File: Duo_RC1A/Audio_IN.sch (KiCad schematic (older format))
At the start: 126 parts, among them J1 JACK_P10_TRS_6P, J2 JACK_P10_TRS_6P

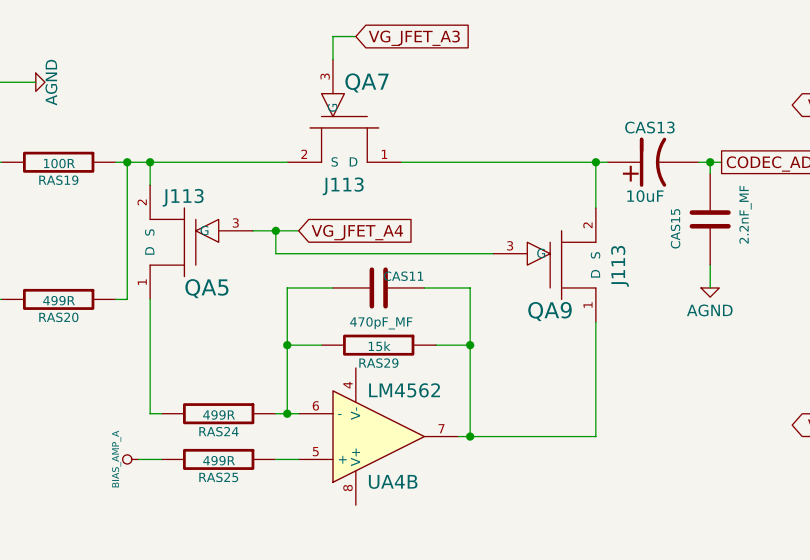
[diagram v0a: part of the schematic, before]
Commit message: PCB dimensions and group placement of all footprints on both BottomBoard and TopBoard layouts.
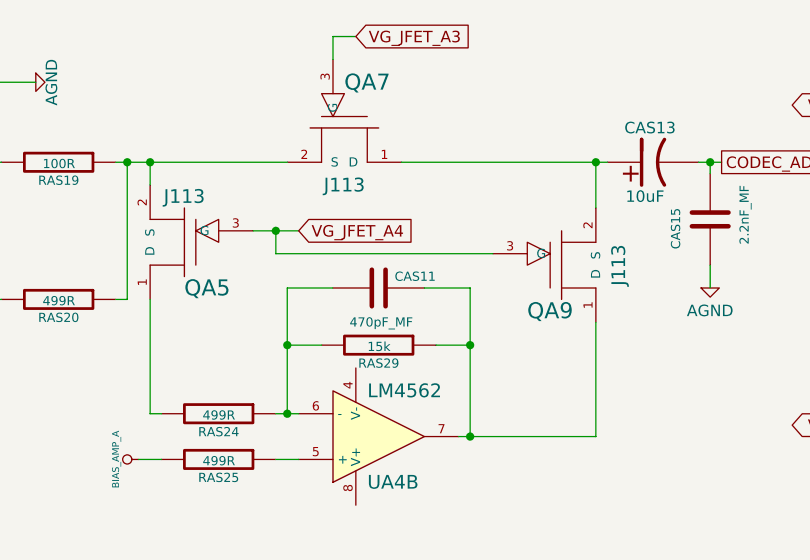
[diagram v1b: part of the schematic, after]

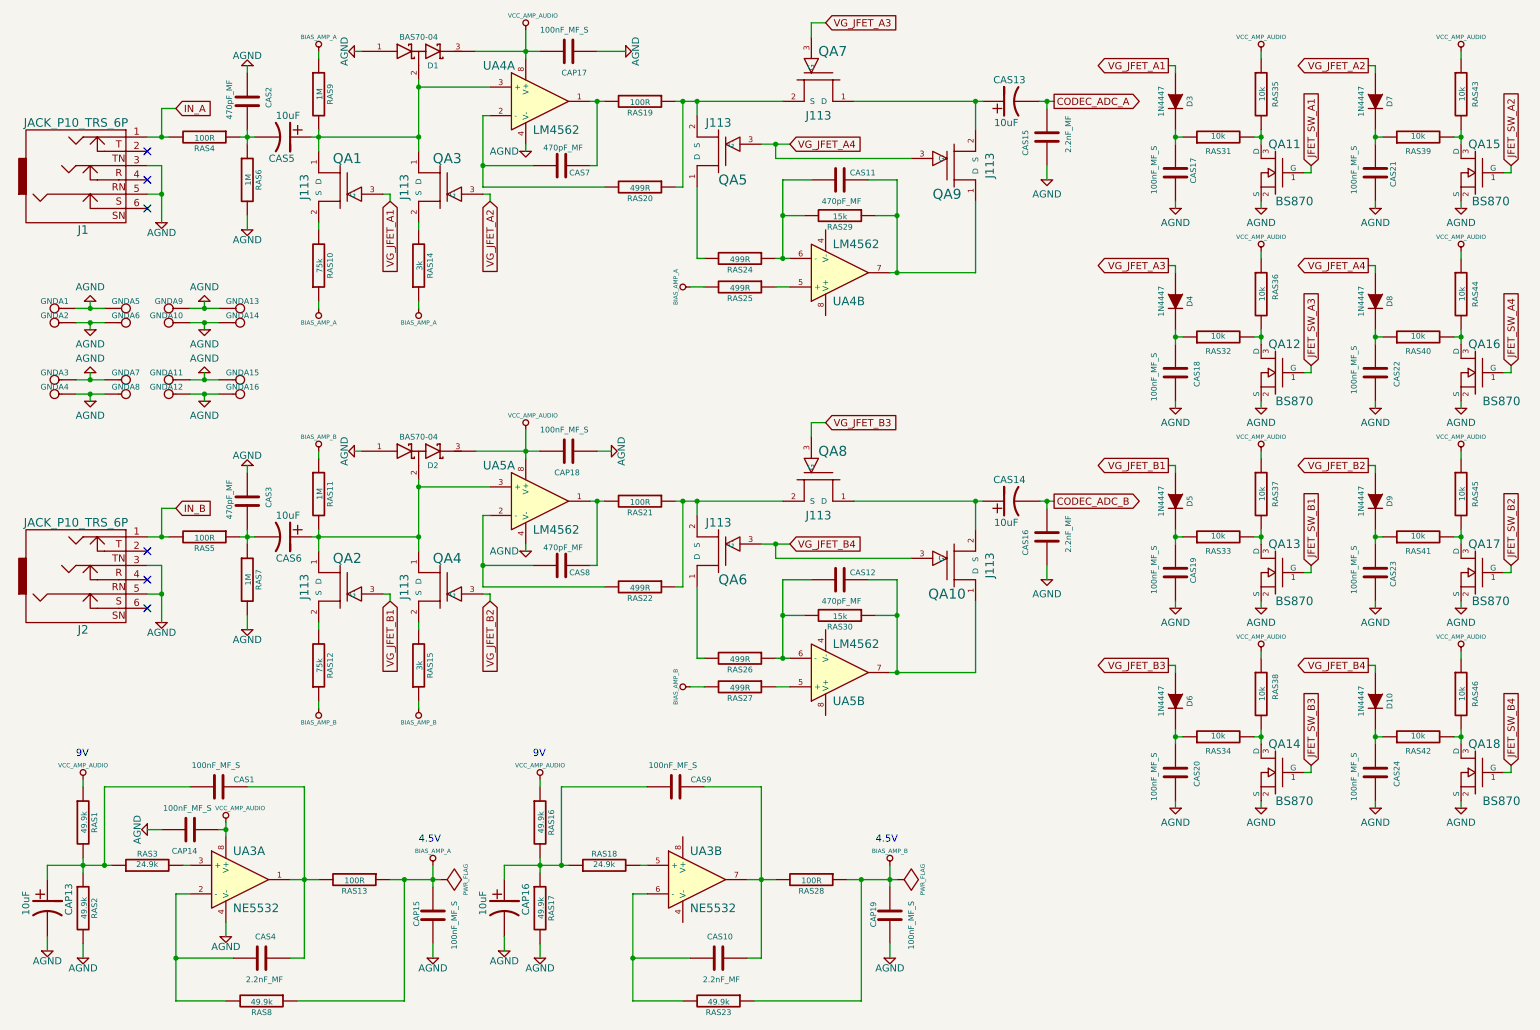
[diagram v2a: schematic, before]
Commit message: Rear pannel layout finished. First layout of sound modules.
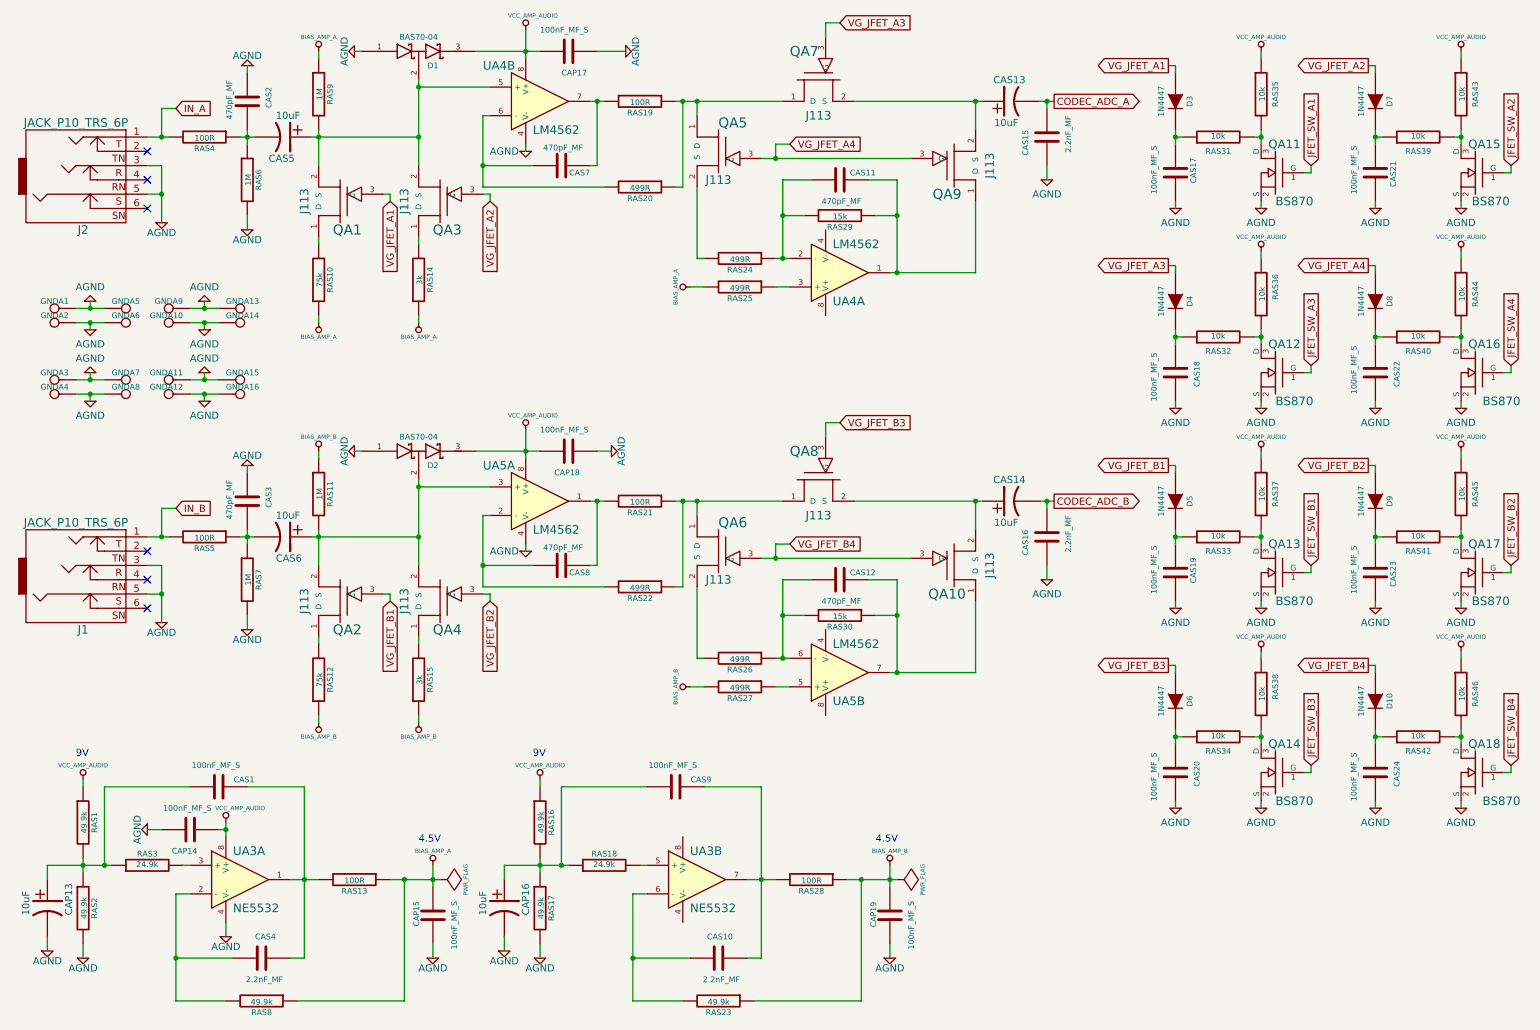
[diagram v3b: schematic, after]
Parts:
- renumbered J2 to J1, J1 to J2
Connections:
- net at CAS7.2, RAS19.2: now also UA4.7; no longer UA4.1
- net at CAS7.1, RAS20.2: now also UA4.6 (-); no longer UA4.2 (-)
- net at CAS5.1, D1.2 (AK), RAS9.2: now also QA1.2 (S), QA3.2 (S), UA4.5 (+); no longer QA1.1 (D), QA3.1 (D), UA4.3 (+)
- net at RAS10.2: now also QA1.1 (D); no longer QA1.2 (S)
- net at RAS14.2: now also QA3.1 (D); no longer QA3.2 (S)
- net at RAS25.1: now also UA4.3 (+); no longer UA4.5 (+)
- net at CAS11.1, RAS24.1, RAS29.2: now also UA4.2 (-); no longer UA4.6 (-)
- net at CAS11.2, QA9.1 (D), RAS29.1: now also UA4.1; no longer UA4.7
- net at RAS19.1, RAS20.1: now also QA5.1 (D), QA7.1 (D); no longer QA5.2 (S), QA7.2 (S)
- net at CAS13.1, QA9.2 (S): now also QA7.2 (S); no longer QA7.1 (D)
- net at RAS24.2: now also QA5.2 (S); no longer QA5.1 (D)
- net at CAS6.1, D2.2 (AK), RAS11.2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: now also QA2.2 (S), QA4.2 (S); no longer QA2.1 (D), QA4.1 (D)
- net at RAS12.2: now also QA2.1 (D); no longer QA2.2 (S)
- net at RAS15.2: now also QA4.1 (D); no longer QA4.2 (S)
- net at RAS26.2: now also QA6.2 (S); no longer QA6.1 (D)
- net at CAS14.1, QA10.2 (S): now also QA8.2 (S); no longer QA8.1 (D)
- net at RAS21.1, RAS22.1: now also QA6.1 (D), QA8.1 (D); no longer QA6.2 (S), QA8.2 (S)
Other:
- moved on the sheet: QA1, QA2, QA3, QA4, RAS10, RAS12, RAS14, RAS15

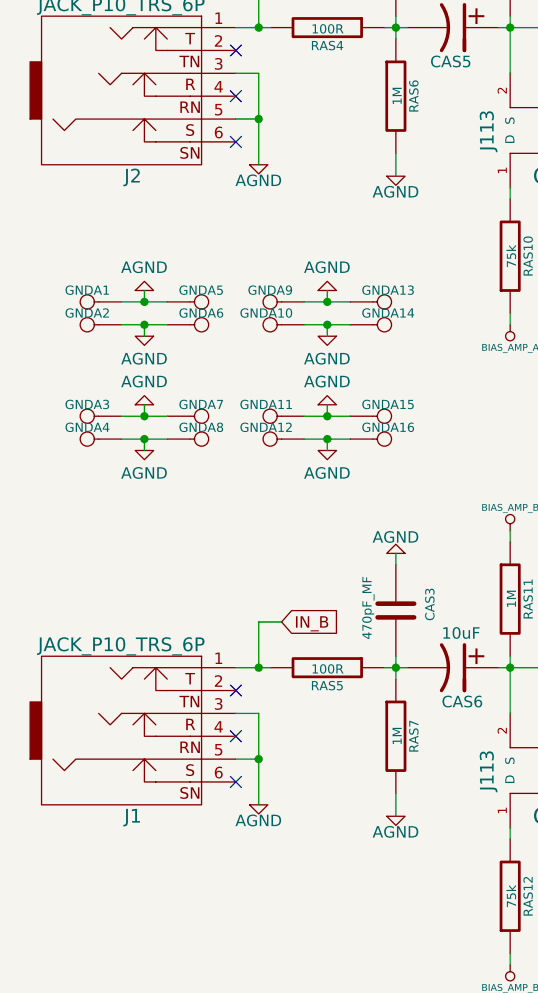
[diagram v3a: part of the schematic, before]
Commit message: Finished the CODEC modular layout. Reduced the space for the Audio Input modular layout.
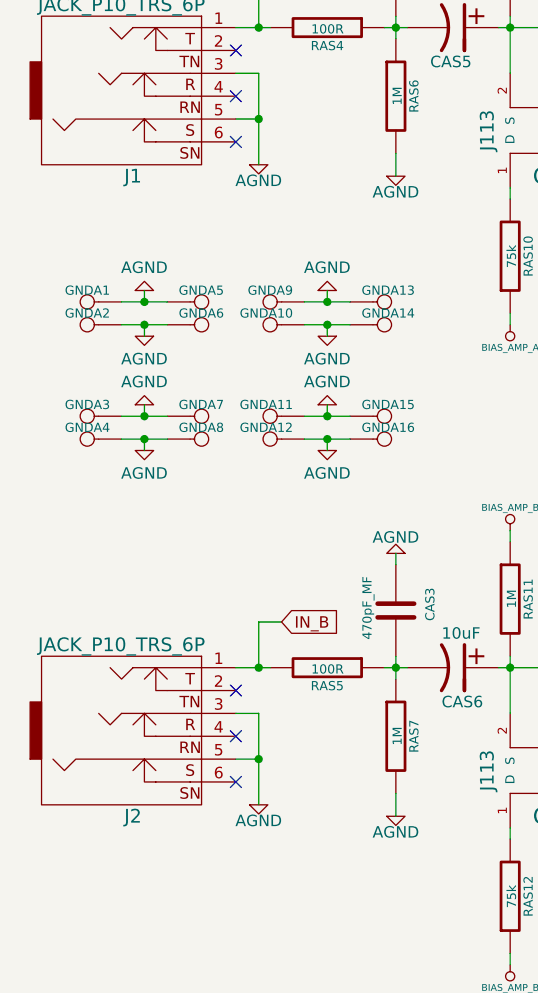
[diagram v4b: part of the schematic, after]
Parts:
- renumbered J2 to J1, J1 to J2
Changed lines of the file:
@@
 IN_A
 $Comp
-L JACK_P10_TRS_6P J2
+L JACK_P10_TRS_6P J1
 U 1 1 533E52E6
 P 1000 1650
-F 0 "J2" H 1000 2050 60  0000 C CNN
+F 0 "J1" H 1000 2050 60  0000 C CNN
 F 1 "JACK_P10_TRS_6P" H 950 1300 60  0000 C CNN
 F 2 "Duo_Audio_HMI_RC1A:JACK-NMJ6HCD2_1" H 1000 1650 60  0001 C CNN
@@
 IN_B
 $Comp
-L JACK_P10_TRS_6P J1
+L JACK_P10_TRS_6P J2
 U 1 1 536AB844
 P 1000 4450
-F 0 "J1" H 1000 4850 60  0000 C CNN
+F 0 "J2" H 1000 4850 60  0000 C CNN
 F 1 "JACK_P10_TRS_6P" H 950 4100 60  0000 C CNN
 F 2 "Duo_Audio_HMI_RC1A:JACK-NMJ6HCD2_1" H 1000 4450 60  0001 C CNN
